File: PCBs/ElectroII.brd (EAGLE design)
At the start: 114.3 x 76.2 mm, 15 parts, among them J1 U.FL-R-SMT(01), U1 RFM95W-868S2

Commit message: Lots of progress on boost converter
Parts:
- added C2: 100u, RTR Main Library:C1206
- added C3: 10u, RTR Main Library:C1206
- added CN1: (no value), adafruit:JST-PH-2-SMT-RA
- added D1: 1N4004, adafruit:DO41-10
- added L1: 6.8u, RTR Main Library:L-DS75LC
- added LOBAT: RED, RTR Main Library:LED5MM
- added PWR: GRN, RTR Main Library:LED5MM
- added R1: 1.85M, RTR Main Library:R1206
- added R2, R4: 200k, RTR Main Library:R1206
- added R3: 1.1M, RTR Main Library:R1206
- added R5, R6: (no value), RTR Main Library:R1206
- added U2: TPS61090RSAR, TPS61090RSAR:QFN65P400X400X100-17N
- moved U$1 8.03 mm to (31.8, 25.4)
- moved I2C0_BRK 7.62 mm to (12.7, 69.8)
- moved I2C0 6.35 mm to (29.2, 76.2)
- moved SPI1 3.81 mm to (67.3, 0.00)
- moved UART0 3.81 mm to (95.2, 76.2)
- moved SPI0 3.81 mm to (62.2, 76.2)
- moved SPI1_BRK 3.81 mm to (83.8, 6.35)
- moved UART0_BRK 3.81 mm to (78.7, 69.8)
- moved I2C1_BRK 2.54 mm to (50.8, 6.35)
- moved SPI0_BRK 2.54 mm to (45.7, 69.8)
- moved I2C1 1.27 mm to (34.3, 0.00)
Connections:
- new net FB: R1.1, R2.2, U2.14
- new net LBI: R3.1, R4.2, U2.9
- new net N$1: LOBAT.A, R6.1
- new net N$2: LOBAT.K, U2.12
- new net N$4: L1.P$2, U2.3, U2.4
- new net N$5: PWR.K, R5.2
- new net VBAT: C3.1, D1.C, L1.P$1, R3.2, U2.11, U2.8
- net GND: now also C2.2, C3.2, CN1.2, D1.A, R2.1, R4.1, R5.1, U2.10, U2.13, U2.17, U2.5, U2.6, U2.7, U2.P$1, U2.P$2, U2.P$3, U2.P$4
- net VCC: now also C2.1, PWR.A, R1.2, R6.2, U2.1, U2.15, U2.16

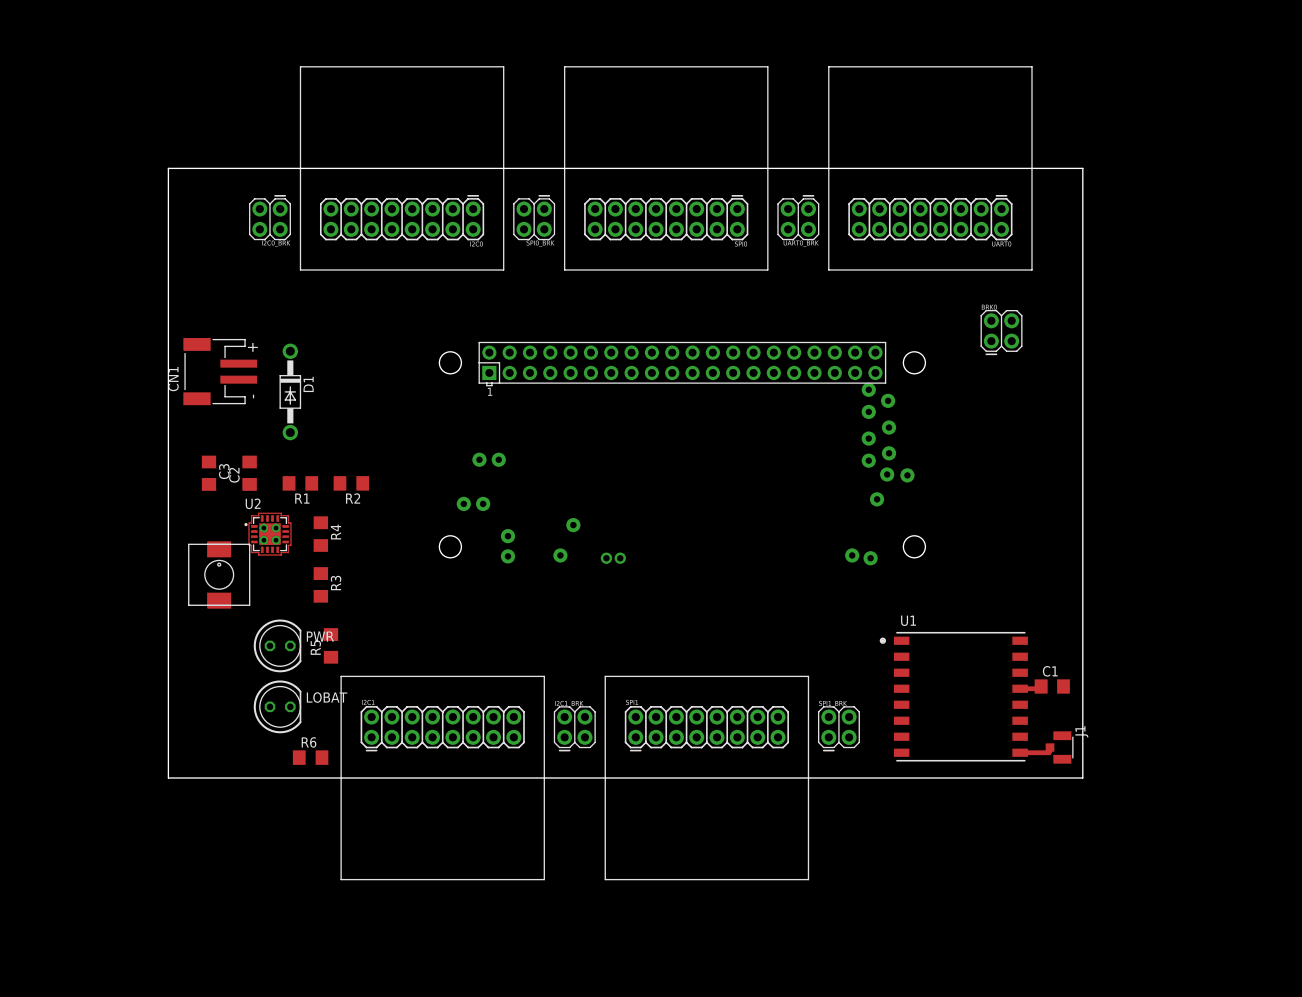
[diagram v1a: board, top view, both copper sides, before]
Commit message: More details on boost converter
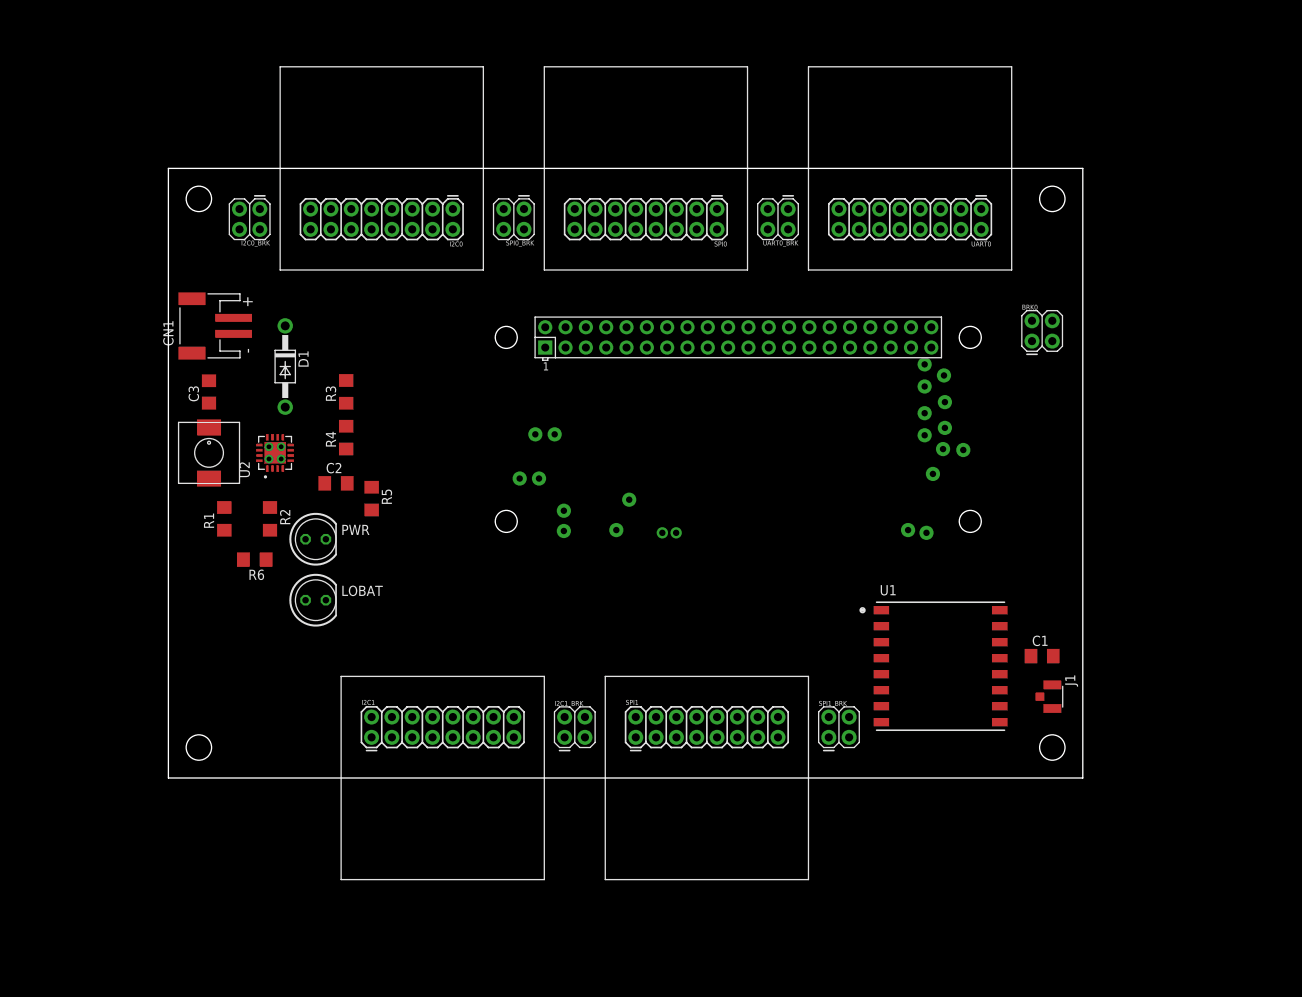
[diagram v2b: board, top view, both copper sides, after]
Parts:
- moved R6 25.7 mm to (10.8, 27.3), turned to 180 degrees
- moved R3 24.3 mm to (22.2, 48.3), turned to 90 degrees
- moved R5 19.1 mm to (25.4, 34.9), turned to 270 degrees
- moved L1 15.3 mm to (5.08, 40.6)
- moved LOBAT 14.1 mm to (18.4, 22.2)
- moved PWR 14.1 mm to (18.4, 29.8)
- moved R4 12.5 mm to (22.2, 42.5), turned to 90 degrees
- moved R2 11.1 mm to (12.7, 32.4), turned to 270 degrees
- moved C2 10.9 mm to (21.0, 36.8), turned to 0 degrees
- moved R1 10.5 mm to (6.99, 32.4), turned to 90 degrees
- moved U2 10.2 mm to (13.3, 40.6), turned to 90 degrees
- moved C3 10.2 mm to (5.08, 48.3), turned to 90 degrees
- moved U$1 7.67 mm to (38.7, 28.6)
- moved J1 6.48 mm to (110.5, 10.2)
- moved CN1 5.75 mm to (4.45, 56.5)
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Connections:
- new net VIN: CN1.1
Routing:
- net ANT: track 4.40 -> 0.00 mm
- net VCC: track 2.90 -> 0.00 mm

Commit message: Concept trace layouts
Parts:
- added F1: NANOSMDC110F-2, NANOSMDC110F-2:RESC3115X65N
- moved R2 9.16 mm to (5.08, 27.3), turned to 180 degrees
- moved D1 6.29 mm to (19.1, 55.9)
- moved R6 4.26 mm to (12.7, 31.1), turned to 90 degrees
- moved R1 2.01 mm to (5.08, 33.0), turned to 0 degrees
- moved J1 1.27 mm to (109.2, 10.2)
- moved C1 0.90 mm to (108.6, 15.9)
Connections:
- net 5V: now also C2.1, PWR.A, R1.2, R6.2, U2.1, U2.15, U2.16
- net VBAT: now also F1.2
- net VCC: no longer C2.1, PWR.A, R1.2, R6.2, U2.1, U2.15, U2.16
- net VIN: now also F1.1
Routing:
- net VCC: track 0.00 -> 279.1 mm, vias 0 -> 2
- net 5V: track 0.00 -> 214.8 mm
- net VBAT: track 0.00 -> 49.8 mm
- net N$2: track 0.00 -> 44.8 mm
- net FB: track 0.00 -> 21.3 mm
- net LBI: track 0.00 -> 12.0 mm, vias 0 -> 2
- net N$4: track 0.00 -> 11.6 mm, vias 0 -> 2
- net N$1: track 0.00 -> 9.31 mm
- net N$5: track 0.00 -> 7.23 mm
- net ANT: track 0.00 -> 5.98 mm
- net VIN: track 0.00 -> 5.15 mm

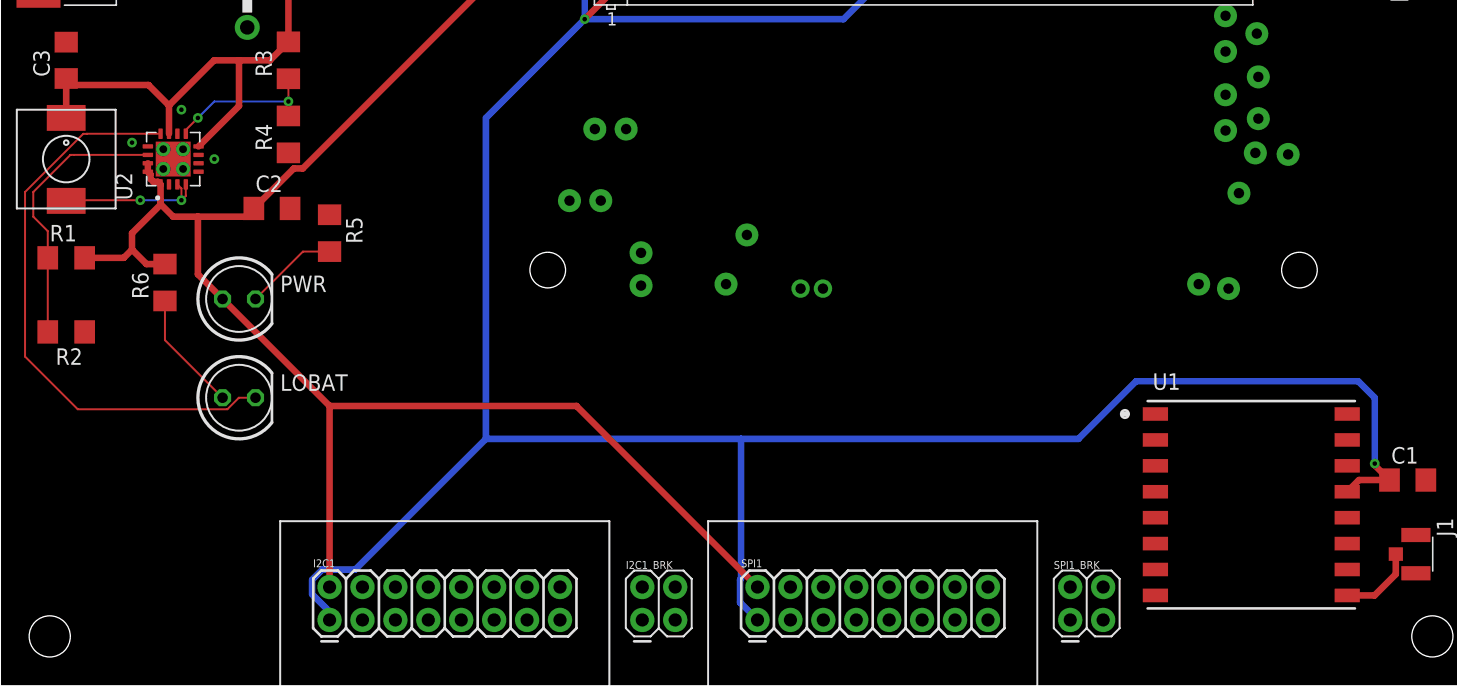
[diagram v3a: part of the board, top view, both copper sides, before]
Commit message: Working on ground plane concept
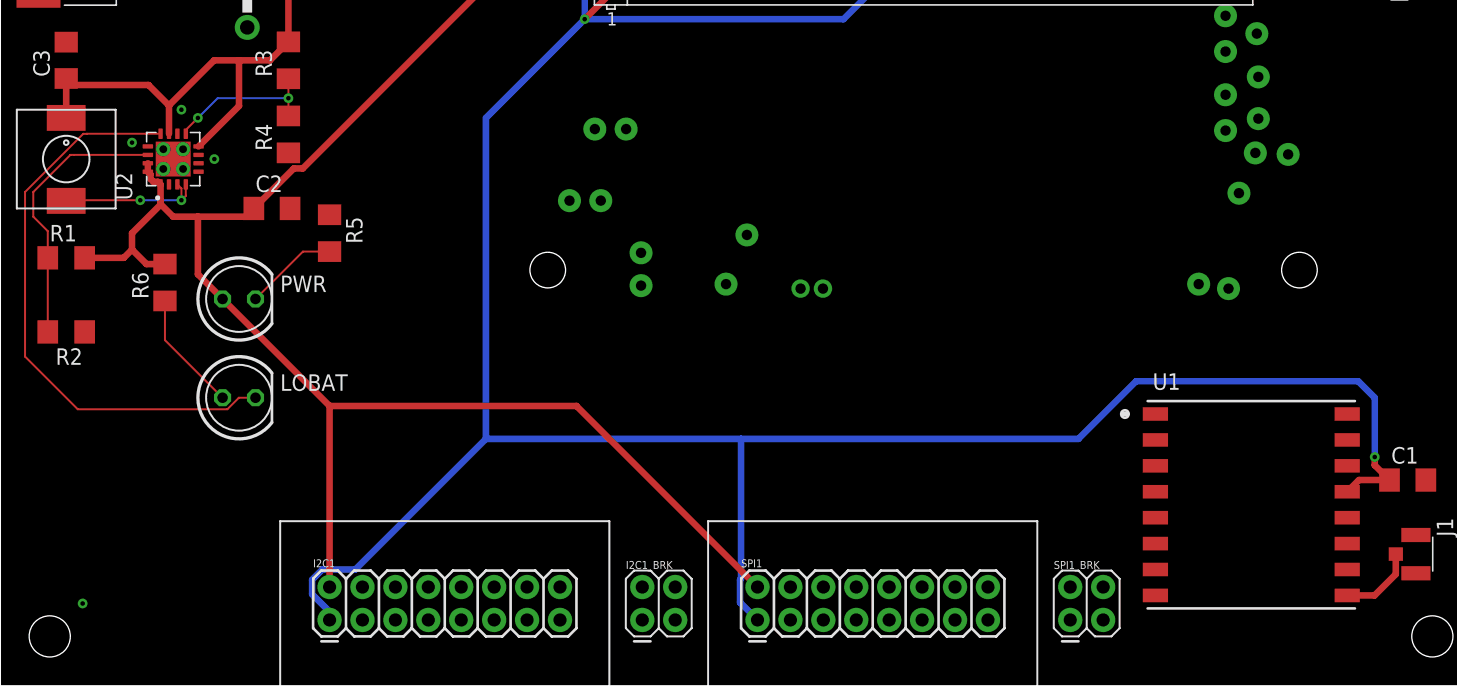
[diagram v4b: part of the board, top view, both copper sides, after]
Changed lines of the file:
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@@
 <setting verticaltext="up"/>
 </settings>
-<grid distance="25" unitdist="mil" unit="mil" style="lines" multiple="1" display="no" altdistance="5" altunitdist="mil" altunit="mil"/>
+<grid distance="10" unitdist="mil" unit="mil" style="lines" multiple="1" display="no" altdistance="5" altunitdist="mil" altunit="mil"/>
 <layers>
 <layer number="1" name="Top" color="4" fill="1" visible="yes" active="yes"/>
@@
 <contactref element="CN1" pad="2"/>
 <via x="13.97" y="44.45" extent="1-16" drill="0.35"/>
+<via x="6.35" y="6.35" extent="1-16" drill="0.35"/>
 <wire x1="87.745" y1="56.345" x2="88.9" y2="71.12" width="0" layer="19" extent="1-1"/>
 <wire x1="82.665" y1="56.345" x2="87.745" y2="56.345" width="0" layer="19" extent="1-1"/>
@@
 <wire x1="8.145" y1="55.515" x2="5.08" y2="49.66" width="0" layer="19" extent="1-1"/>
 <wire x1="6.502" y1="27.305" x2="12.573" y2="39.878" width="0" layer="19" extent="1-1"/>
-<wire x1="89.12" y1="20.97" x2="95.365" y2="53.805" width="0" layer="19" extent="1-1"/>
-<wire x1="89.12" y1="6.97" x2="89.12" y2="20.97" width="0" layer="19" extent="1-1"/>
+<wire x1="6.35" y1="6.35" x2="6.502" y2="27.305" width="0" layer="19" extent="1-1"/>
+<wire x1="38.1" y1="5.08" x2="6.35" y2="6.35" width="0" layer="19" extent="1-1"/>
+<wire x1="71.12" y1="5.08" x2="38.1" y2="5.08" width="0" layer="19" extent="1-1"/>
+<wire x1="89.12" y1="6.97" x2="71.12" y2="5.08" width="0" layer="19" extent="1-1"/>
+<wire x1="89.12" y1="20.97" x2="89.12" y2="6.97" width="0" layer="19" extent="1-1"/>
 <wire x1="103.92" y1="8.97" x2="89.12" y2="6.97" width="0" layer="19" extent="1-1"/>
 <wire x1="109.22" y1="8.685" x2="103.92" y2="8.97" width="0" layer="19" extent="1-1"/>
 <wire x1="109.22" y1="11.635" x2="109.22" y2="8.685" width="0" layer="19" extent="1-1"/>
 <wire x1="109.985" y1="15.875" x2="109.22" y2="11.635" width="0" layer="19" extent="1-1"/>
-<wire x1="71.12" y1="5.08" x2="89.12" y2="6.97" width="0" layer="19" extent="1-1"/>
-<wire x1="38.1" y1="5.08" x2="71.12" y2="5.08" width="0" layer="19" extent="1-1"/>
 </signal>
 <signal name="MOSI">
@@
 <wire x1="87.63" y1="23.495" x2="104.775" y2="23.495" width="0.508" layer="16"/>
 <wire x1="104.775" y1="23.495" x2="106.045" y2="22.225" width="0.508" layer="16"/>
-<wire x1="106.045" y1="22.225" x2="106.045" y2="17.145" width="0.508" layer="16"/>
-<via x="106.045" y="17.145" extent="1-16" drill="0.35"/>
-<wire x1="106.045" y1="17.145" x2="106.045" y2="17.015" width="0.508" layer="1"/>
+<wire x1="106.045" y1="22.225" x2="106.045" y2="17.653" width="0.508" layer="16"/>
+<via x="106.045" y="17.653" extent="1-16" drill="0.35"/>
+<wire x1="106.045" y1="17.653" x2="106.045" y2="17.015" width="0.508" layer="1"/>
 <wire x1="106.045" y1="17.015" x2="107.185" y2="15.875" width="0.508" layer="1"/>
 <wire x1="103.92" y1="14.97" x2="104.825" y2="15.875" width="0.508" layer="1"/>
@@
 <wire x1="14.31" y1="42.595" x2="14.31" y2="42.885" width="0.1524" layer="1"/>
 <wire x1="14.31" y1="42.885" x2="15.24" y2="43.815" width="0.1524" layer="1"/>
-<wire x1="15.24" y1="43.815" x2="16.51" y2="45.085" width="0.1524" layer="16"/>
-<wire x1="16.51" y1="45.085" x2="22.225" y2="45.085" width="0.1524" layer="16"/>
-<via x="22.225" y="45.085" extent="1-16" drill="0.35"/>
-<wire x1="22.225" y1="45.085" x2="22.225" y2="43.967" width="0.1524" layer="1"/>
-<wire x1="22.225" y1="45.085" x2="22.225" y2="46.838" width="0.1524" layer="1"/>
+<wire x1="15.24" y1="43.815" x2="16.764" y2="45.339" width="0.1524" layer="16"/>
+<wire x1="16.764" y1="45.339" x2="22.225" y2="45.339" width="0.1524" layer="16"/>
+<via x="22.225" y="45.339" extent="1-16" drill="0.35"/>
+<wire x1="22.225" y1="45.339" x2="22.225" y2="43.967" width="0.1524" layer="1"/>
+<wire x1="22.225" y1="45.339" x2="22.225" y2="46.838" width="0.1524" layer="1"/>
 </signal>
 <signal name="N$4">
